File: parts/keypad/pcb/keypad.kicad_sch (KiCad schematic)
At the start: 14 parts, among them J1 Conn_02x10_Top_Bottom, J2 1x10, J3 To SENSOR HUB, J4 To DISPLAY MODULE, SW1 SW_Push, SW10 SW_Push, SW2 SW_Push, SW3 SW_Push, SW4 SW_Push, SW5 SW_Push, SW6 SW_Push, SW7 SW_Push, SW8 SW_Push, SW9 SW_Push

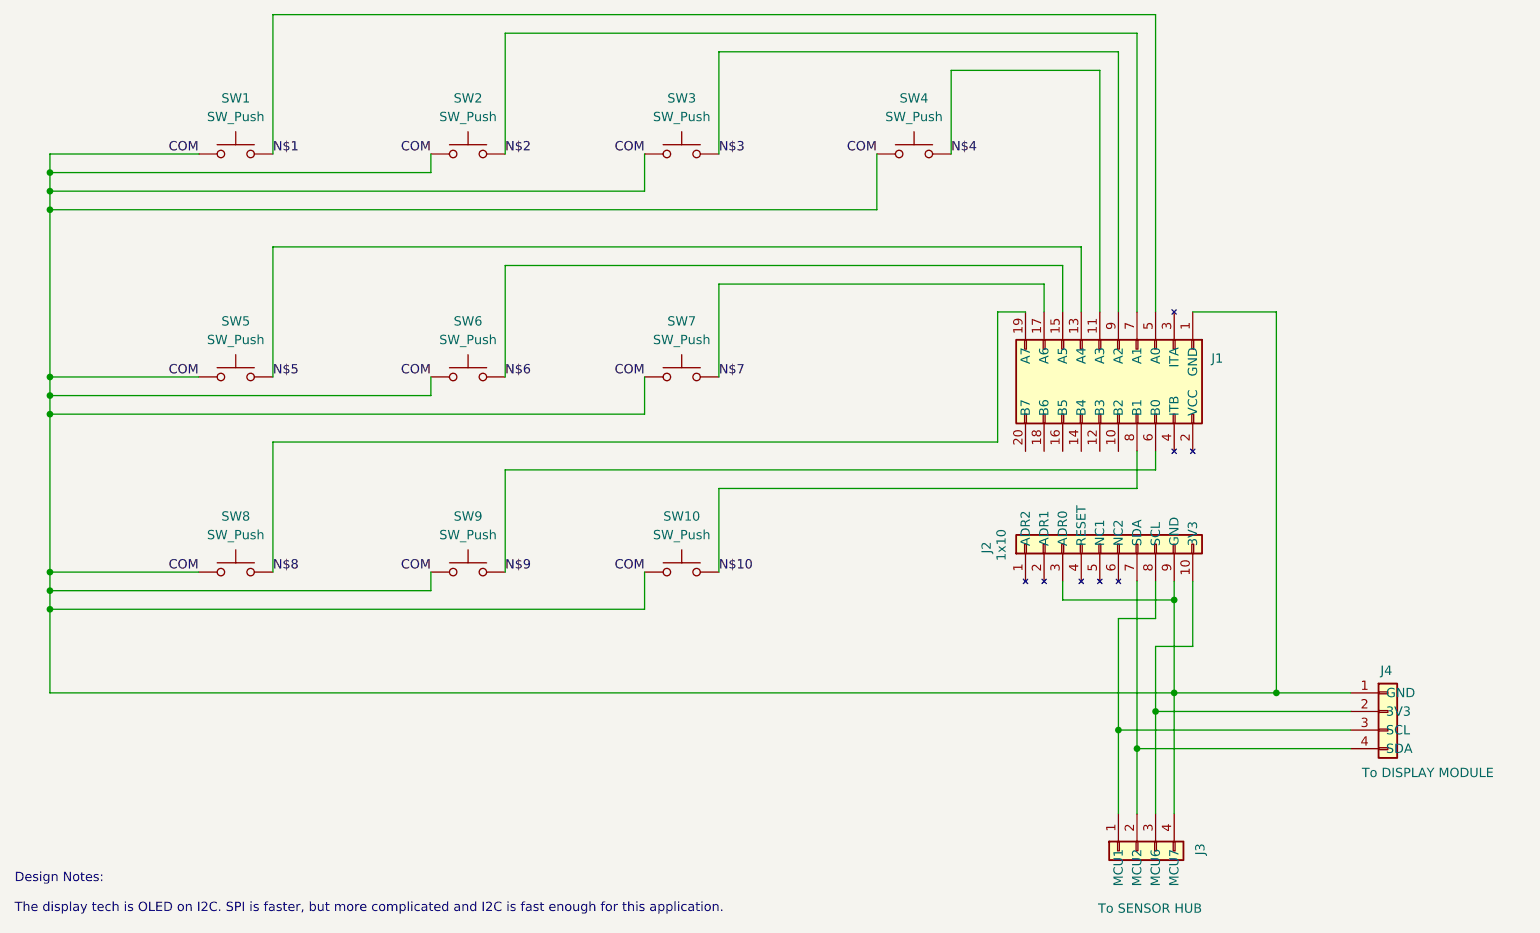
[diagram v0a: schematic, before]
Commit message: revise keypad due to soldering screw up (now rev 1.6); add todo notes.
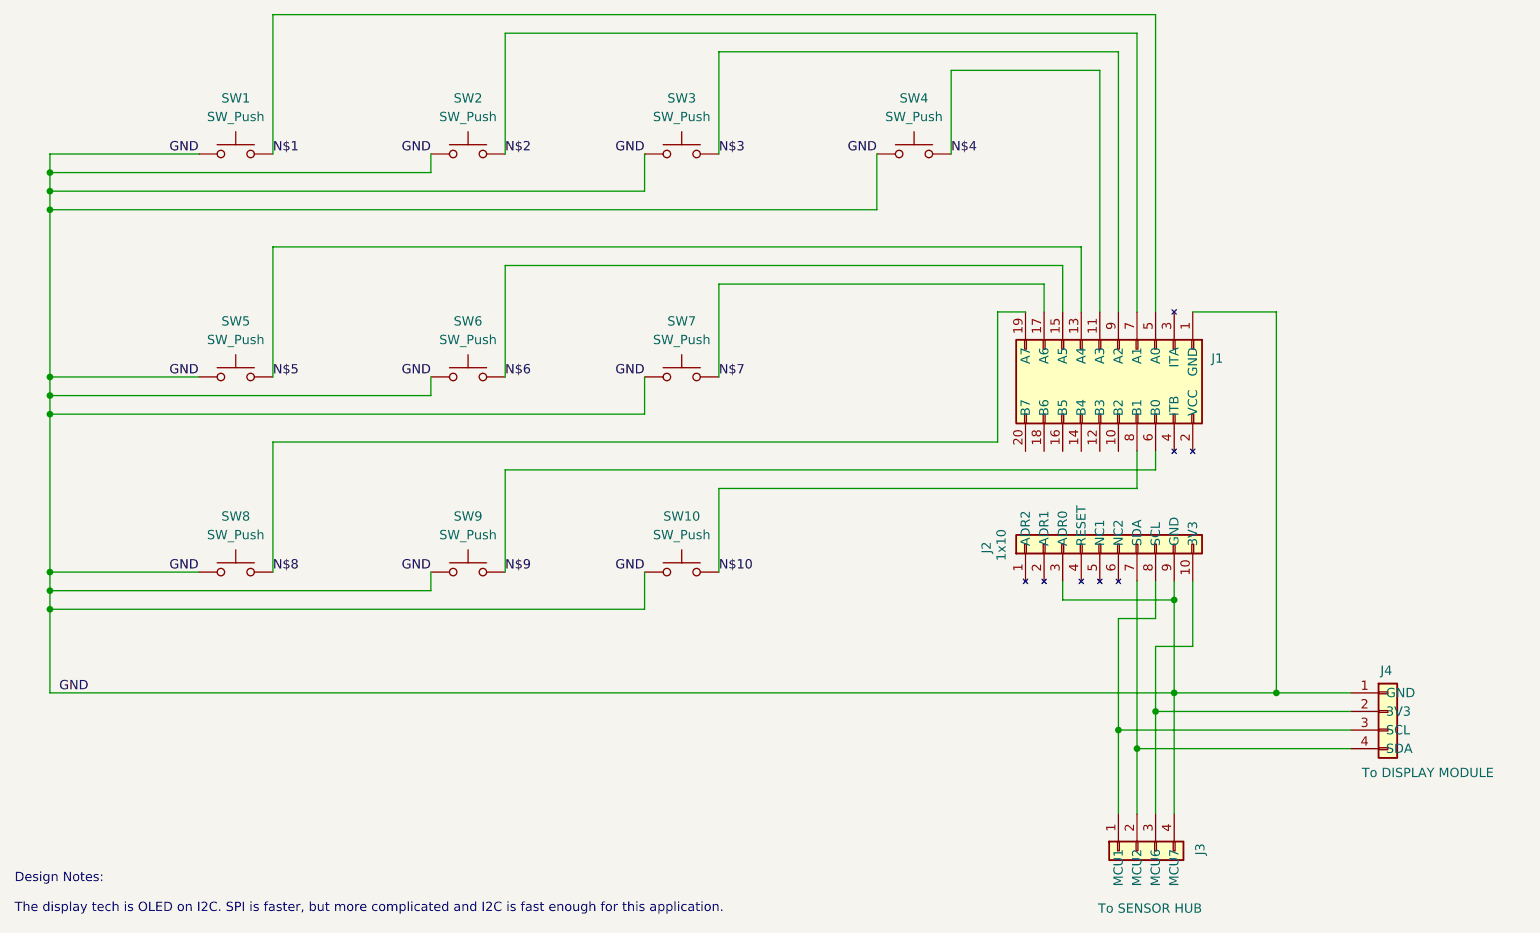
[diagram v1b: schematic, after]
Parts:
- J4: footprint Connector_PinSocket_2.54mm:PinSocket_1x04_P2.54mm_Vertical -> Connector_PinHeader_2.54mm:PinHeader_1x04_P2.54mm_Horizontal
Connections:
- net COM renamed GND
